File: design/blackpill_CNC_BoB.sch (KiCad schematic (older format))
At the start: 295 parts, among them J101 ALimIN, J102 ZLimIN, J103 YLimIN, J104 XLimIN, J105 CS_IN, J106 FH_IN, J107 DoorIN, J108 ResetIN, J109 ProbeIN, J110 12V Power in, J111 AuxEncIn, J112 5V Power out, J113 ADC_in_1, J114 ADC_in_2, J115 stepDriverLim, J116 Reset, J117 UART1, J118 I2C, J119 SpindleVFD, J120 Spindle/Coolant, J121 Spindle, J122 Coolant, J123 AuxOut, J124 XStepDrv, J125 YStepDrv, J126 ZStepDrv, J127 AStepDrv, U101 TLP290-4, U102 TLP290-4, U103 TLP290-4, U104 74LVC2G17, U105 LD1117S50TR_SOT223, U106 LM358, U107 TLV9001, U108 TLV9001, U109 YAAJ_WeAct_BlackPill_Part_Like, U110 TLV9001, U111 TLV9001, U112 74HCT541, U113 74HCT541, U114 74HCT541, U115 ULN2003A, U116 ULN2003A, U117 ULN2003A

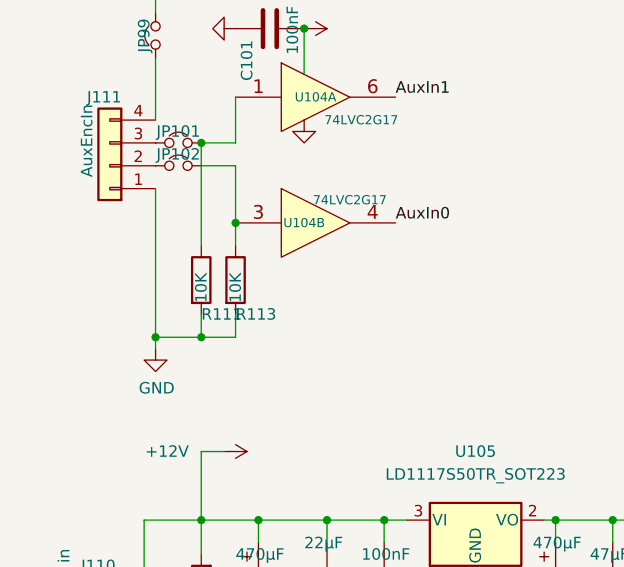
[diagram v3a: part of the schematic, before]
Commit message: rework BOM and correct quite some errors
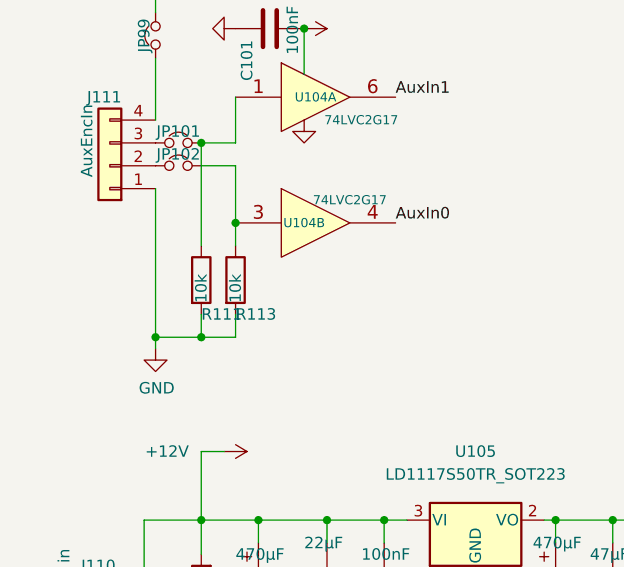
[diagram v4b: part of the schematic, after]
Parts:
- D114: footprint Connector_Phoenix_MSTB:PhoenixContact_MSTBA_2,5_2-G-5,08_1x02_P5.08mm_Horizontal -> LED_SMD:LED_0603_1608Metric
- R111, R113: value 10K -> 10k
- R140, R141, R142, R144, R145, R146, R147, R148: footprint Resistor_SMD:R_0201_0603Metric -> Resistor_SMD:R_0603_1608Metric
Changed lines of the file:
@@
 P 1550 8800
 F 0 "R113" H 1550 8650 50  0000 L CNN
-F 1 "10K" V 1550 8700 50  0000 L CNN
+F 1 "10k" V 1550 8700 50  0000 L CNN
 F 2 "Resistor_SMD:R_0603_1608Metric" V 1480 8800 50  0001 C CNN
 F 3 "~" H 1550 8800 50  0001 C CNN
@@
 P 1400 8800
 F 0 "R111" H 1400 8650 50  0000 L CNN
-F 1 "10K" V 1400 8700 50  0000 L CNN
+F 1 "10k" V 1400 8700 50  0000 L CNN
 F 2 "Resistor_SMD:R_0603_1608Metric" V 1330 8800 50  0001 C CNN
 F 3 "~" H 1400 8800 50  0001 C CNN
@@
 F 0 "D114" H 13600 9250 50  0000 C CNN
 F 1 "LED" H 13500 9050 50  0001 C CNN
-F 2 "Connector_Phoenix_MSTB:PhoenixContact_MSTBA_2,5_2-G-5,08_1x02_P5.08mm_Horizontal" H 13550 9250 50  0001 C CNN
+F 2 "LED_SMD:LED_0603_1608Metric" H 13550 9250 50  0001 C CNN
 F 3 "~" H 13550 9250 50  0001 C CNN
 	1    13550 9250
@@
 F 0 "R148" V 10150 9850 50  0000 C CNN
 F 1 "10k" V 10250 9850 50  0000 C CNN
-F 2 "Resistor_SMD:R_0201_0603Metric" V 10180 9850 50  0001 C CNN
+F 2 "Resistor_SMD:R_0603_1608Metric" V 10180 9850 50  0001 C CNN
 F 3 "~" H 10250 9850 50  0001 C CNN
 	1    10250 9850
@@
 F 0 "R145" V 9150 10250 50  0000 C CNN
 F 1 "10k" V 9250 10250 50  0000 C CNN
-F 2 "Resistor_SMD:R_0201_0603Metric" V 9180 10250 50  0001 C CNN
+F 2 "Resistor_SMD:R_0603_1608Metric" V 9180 10250 50  0001 C CNN
 F 3 "~" H 9250 10250 50  0001 C CNN
 	1    9250 10250
@@
 F 0 "R140" V 8650 10250 50  0000 C CNN
 F 1 "10k" V 8750 10250 50  0000 C CNN
-F 2 "Resistor_SMD:R_0201_0603Metric" V 8680 10250 50  0001 C CNN
+F 2 "Resistor_SMD:R_0603_1608Metric" V 8680 10250 50  0001 C CNN
 F 3 "~" H 8750 10250 50  0001 C CNN
 	1    8750 10250
@@
 F 0 "R144" V 9150 9850 50  0000 C CNN
 F 1 "10k" V 9250 9850 50  0000 C CNN
-F 2 "Resistor_SMD:R_0201_0603Metric" V 9180 9850 50  0001 C CNN
+F 2 "Resistor_SMD:R_0603_1608Metric" V 9180 9850 50  0001 C CNN
 F 3 "~" H 9250 9850 50  0001 C CNN
 	1    9250 9850
@@
 F 0 "R141" V 8900 4700 50  0000 L CNN
 F 1 "10k" V 8800 4700 50  0000 L CNN
-F 2 "Resistor_SMD:R_0201_0603Metric" V 8730 4800 50  0001 C CNN
+F 2 "Resistor_SMD:R_0603_1608Metric" V 8730 4800 50  0001 C CNN
 F 3 "~" H 8800 4800 50  0001 C CNN
 	1    8800 4800
@@
 F 0 "R142" V 8900 6450 50  0000 L CNN
 F 1 "10k" V 8800 6450 50  0000 L CNN
-F 2 "Resistor_SMD:R_0201_0603Metric" V 8730 6550 50  0001 C CNN
+F 2 "Resistor_SMD:R_0603_1608Metric" V 8730 6550 50  0001 C CNN
 F 3 "~" H 8800 6550 50  0001 C CNN
 	1    8800 6550
@@
 F 0 "R146" H 9710 7740 50  0000 L CNN
 F 1 "2K2" V 9710 7790 50  0000 L CNN
-F 2 "Resistor_SMD:R_0201_0603Metric" V 9640 7890 50  0001 C CNN
+F 2 "Resistor_SMD:R_0603_1608Metric" V 9640 7890 50  0001 C CNN
 F 3 "~" H 9710 7890 50  0001 C CNN
 	1    9710 7890
@@
 F 0 "R147" H 9850 7740 50  0000 L CNN
 F 1 "2K2" V 9850 7790 50  0000 L CNN
-F 2 "Resistor_SMD:R_0201_0603Metric" V 9780 7890 50  0001 C CNN
+F 2 "Resistor_SMD:R_0603_1608Metric" V 9780 7890 50  0001 C CNN
 F 3 "~" H 9850 7890 50  0001 C CNN
 	1    9850 7890

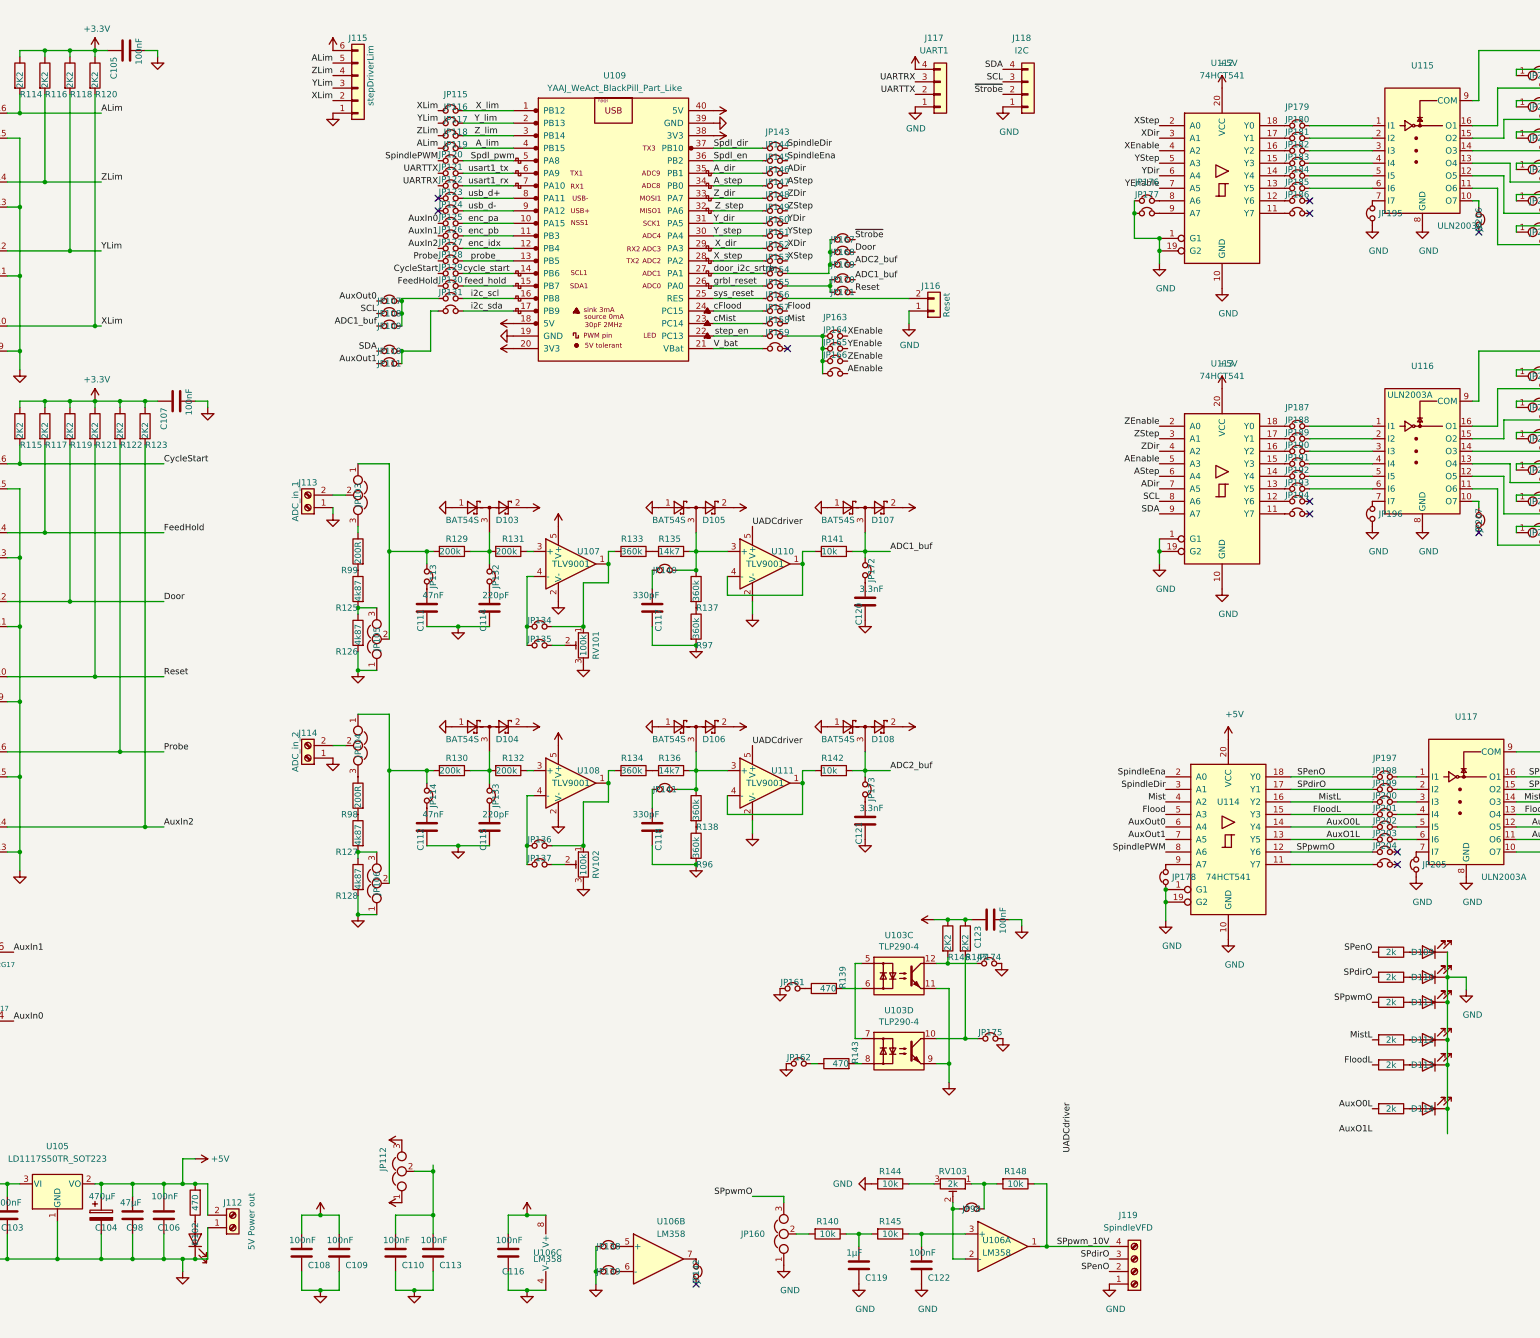
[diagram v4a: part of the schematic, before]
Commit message: presorting digi input and power
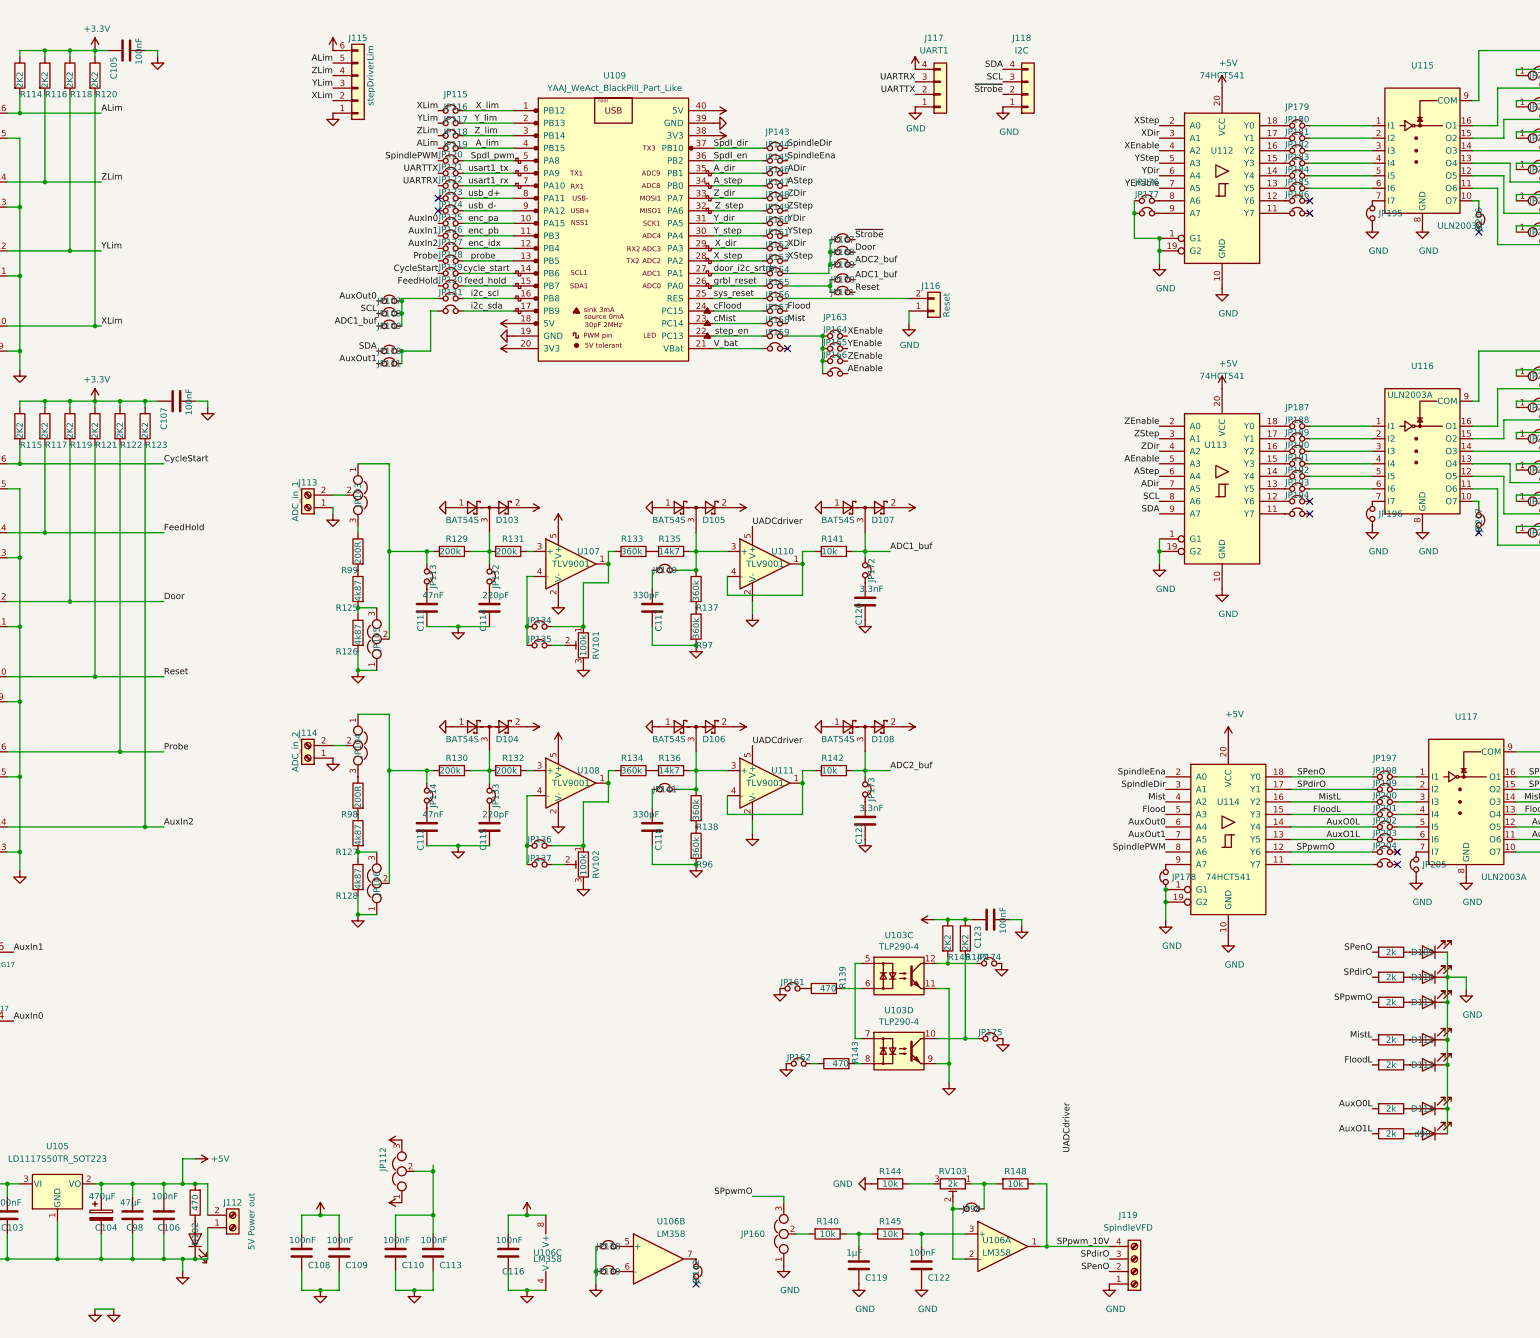
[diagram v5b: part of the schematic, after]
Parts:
- added d90: LED, LED_SMD:LED_0603_1608Metric, symbol Device:LED
- added r90: 2k, Resistor_SMD:R_0603_1608Metric, symbol Device:R
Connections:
- net AuxO1L: now also r90.2
- net GND: now also d90.1 (K)
- new net: d90.2 (A), r90.1
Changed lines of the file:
@@
 U 1 1 6A55287E
 P 11900 1900
-F 0 "U112" H 11900 2900 50  0000 C CNN
+F 0 "U112" H 11900 2200 50  0000 C CNN
 F 1 "74HCT541" H 11900 2800 50  0000 C CNN
 F 2 "Package_SO:TSSOP-20_4.4x6.5mm_P0.65mm" H 11900 1900 50  0001 C CNN
@@
 U 1 1 6A60AB9B
 P 11900 4300
-F 0 "U113" H 11900 5300 50  0000 C CNN
+F 0 "U113" H 11850 4650 50  0000 C CNN
 F 1 "74HCT541" H 11900 5200 50  0000 C CNN
 F 2 "Package_SO:TSSOP-20_4.4x6.5mm_P0.65mm" H 11900 4300 50  0001 C CNN
@@
 	0    1    1    0
 $EndComp
-$Comp
-L power:GNDS #PWR0113
-U 1 1 72B97E1F
-P 3400 850
-F 0 "#PWR0113" H 3400 600 50  0001 C CNN
-F 1 "GNDS" H 3405 677 50  0001 C CNN
-F 2 "" H 3400 850 50  0001 C CNN
-F 3 "" H 3400 850 50  0001 C CNN
-	1    3400 850
-	1    0    0    -1
-$EndComp
 Wire Wire Line
 	2900 800  3000 800
@@
 	7350 7300 7700 7300
 Connection ~ 7700 7300
+$Comp
+L Device:R r90
+U 1 1 67BECA90
+P 13250 9450
+F 0 "r90" V 13000 9450 50  0001 C CNN
+F 1 "2k" V 13250 9450 50  0000 C CNN
+F 2 "Resistor_SMD:R_0603_1608Metric" V 13180 9450 50  0001 C CNN
+F 3 "~" H 13250 9450 50  0001 C CNN
+	1    13250 9450
+	0    1    1    0
+$EndComp
+$Comp
+L Device:LED d90
+U 1 1 67BED2C6
+P 13550 9450
+F 0 "d90" H 13600 9450 50  0000 C CNN
+F 1 "LED" H 13500 9250 50  0001 C CNN
+F 2 "LED_SMD:LED_0603_1608Metric" H 13550 9450 50  0001 C CNN
+F 3 "~" H 13550 9450 50  0001 C CNN
+	1    13550 9450
+	-1   0    0    1
+$EndComp
+$Comp
+L power:GNDS #PWR0113
+U 1 1 72B97E1F
+P 3400 850
+F 0 "#PWR0113" H 3400 600 50  0001 C CNN
+F 1 "GNDS" H 3405 677 50  0001 C CNN
+F 2 "" H 3400 850 50  0001 C CNN
+F 3 "" H 3400 850 50  0001 C CNN
+	1    3400 850
+	1    0    0    -1
+$EndComp
+$Comp
+L power:GNDS #PWR?
+U 1 1 67D8B4F1
+P 2900 10850
+F 0 "#PWR?" H 2900 10600 50  0001 C CNN
+F 1 "GNDS" H 2905 10677 50  0001 C CNN
+F 2 "" H 2900 10850 50  0001 C CNN
+F 3 "" H 2900 10850 50  0001 C CNN
+	1    2900 10850
+	1    0    0    -1
+$EndComp
+$Comp
+L power:GND #PWR?
+U 1 1 67DBA7B6
+P 3050 10850
+F 0 "#PWR?" H 3050 10600 50  0001 C CNN
+F 1 "GND" H 3100 10650 50  0001 C CNN
+F 2 "" H 3050 10850 50  0001 C CNN
+F 3 "" H 3050 10850 50  0001 C CNN
+	1    3050 10850
+	1    0    0    -1
+$EndComp
+Wire Wire Line
+	2900 10850 3050 10850
 $EndSCHEMATC

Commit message: updated J111 correction
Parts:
- J111: footprint Connector_Phoenix_MSTB:PhoenixContact_MSTBA_2,5_2-G-5,08_1x02_P5.08mm_Horizontal -> Connector_PinSocket_2.54mm:PinSocket_1x04_P2.54mm_Vertical
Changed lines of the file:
@@
 F 0 "J111" H 1100 8000 50  0000 R CNN
 F 1 "AuxEncIn" V 1100 8350 50  0000 R CNN
-F 2 "Connector_Phoenix_MSTB:PhoenixContact_MSTBA_2,5_2-G-5,08_1x02_P5.08mm_Horizontal" H 1000 8300 50  0001 C CNN
+F 2 "Connector_PinSocket_2.54mm:PinSocket_1x04_P2.54mm_Vertical" H 1000 8300 50  0001 C CNN
 F 3 "~" H 1000 8300 50  0001 C CNN
 	1    1000 8300
@@
 $EndComp
 $Comp
-L power:GNDS #PWR?
+L power:GNDS #PWR0201
 U 1 1 67D8B4F1
 P 2900 10850
-F 0 "#PWR?" H 2900 10600 50  0001 C CNN
+F 0 "#PWR0201" H 2900 10600 50  0001 C CNN
 F 1 "GNDS" H 2905 10677 50  0001 C CNN
 F 2 "" H 2900 10850 50  0001 C CNN
@@
 $EndComp
 $Comp
-L power:GND #PWR?
+L power:GND #PWR0202
 U 1 1 67DBA7B6
 P 3050 10850
-F 0 "#PWR?" H 3050 10600 50  0001 C CNN
+F 0 "#PWR0202" H 3050 10600 50  0001 C CNN
 F 1 "GND" H 3100 10650 50  0001 C CNN
 F 2 "" H 3050 10850 50  0001 C CNN
